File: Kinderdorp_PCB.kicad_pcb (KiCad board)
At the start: 2 copper layers, 99.1 x 99.1 mm, 44 parts, among them Q1 2N7002_C306856, U1 AMS1117-3.3_C347222, U2 ESP32-C3-WROOM-02-N4(4MB)

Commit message: routing
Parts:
- moved RXD 34.6 mm to (155.6, 123.1)
- moved GND 32.2 mm to (159.7, 123.1)
- moved TXD 30.5 mm to (151.5, 123.0)
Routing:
- net +5V: track 14.4 -> 325.1 mm, vias 0 -> 2
- net GPIO5: track 0.00 -> 100.7 mm, vias 0 -> 1
- net Net-(U2-IO2): track 0.00 -> 70.2 mm, vias 0 -> 1
- net Net-(LED4-DOUT): track 0.00 -> 47.4 mm
- net +3V3: track 83.4 -> 123.7 mm
- net Net-(LED2-DOUT): track 0.00 -> 38.5 mm
- net Net-(LED5-DOUT): track 0.00 -> 37.7 mm
- net Net-(LED7-DOUT): track 0.00 -> 35.6 mm
- net Net-(LED1-DOUT): track 0.00 -> 34.1 mm
- net Net-(LED6-DOUT): track 0.00 -> 32.3 mm
- net Net-(LED3-DOUT): track 0.00 -> 26.7 mm
- net Net-(U2-TXD): track 0.00 -> 18.4 mm
- net Net-(U2-RXD): track 0.00 -> 14.9 mm
- net BUZZ: track 13.9 -> 19.1 mm, vias 0 -> 2
- net Net-(D1-A): track 140.3 -> 138.3 mm

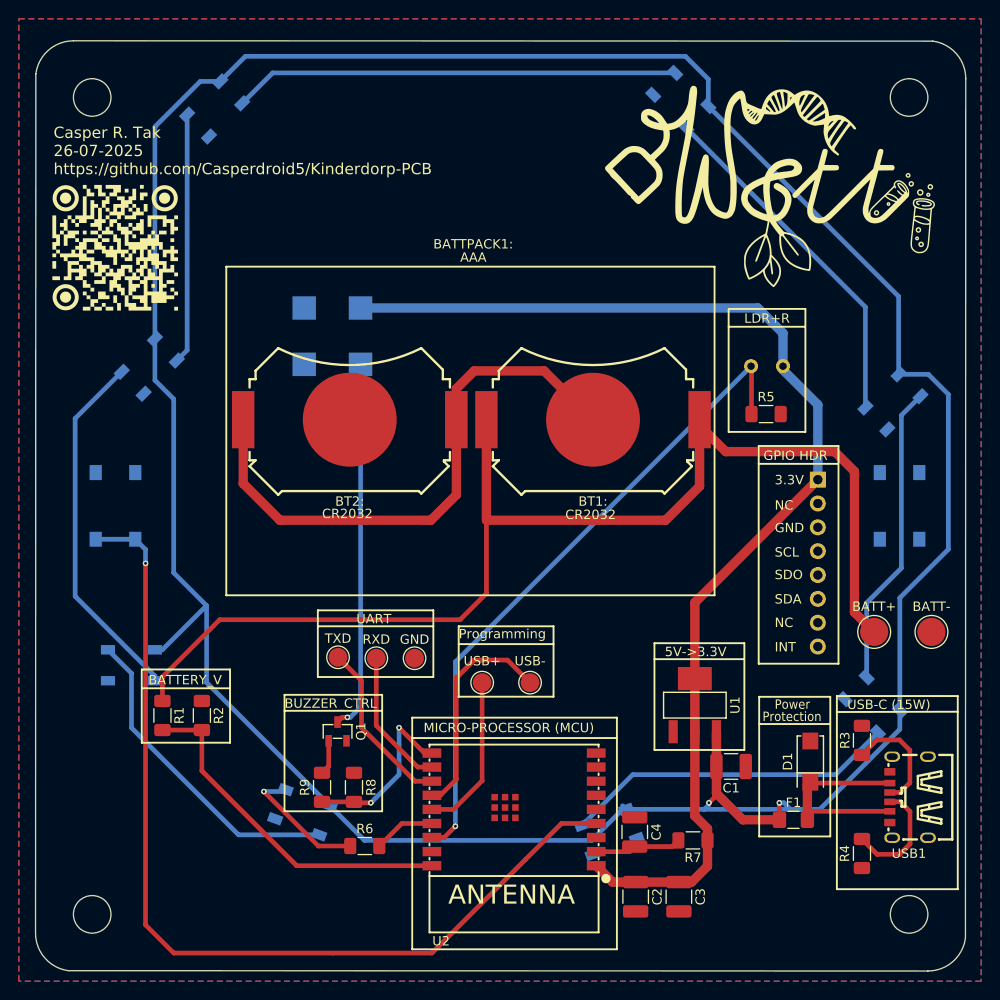
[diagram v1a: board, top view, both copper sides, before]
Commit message: added media files and finished routing
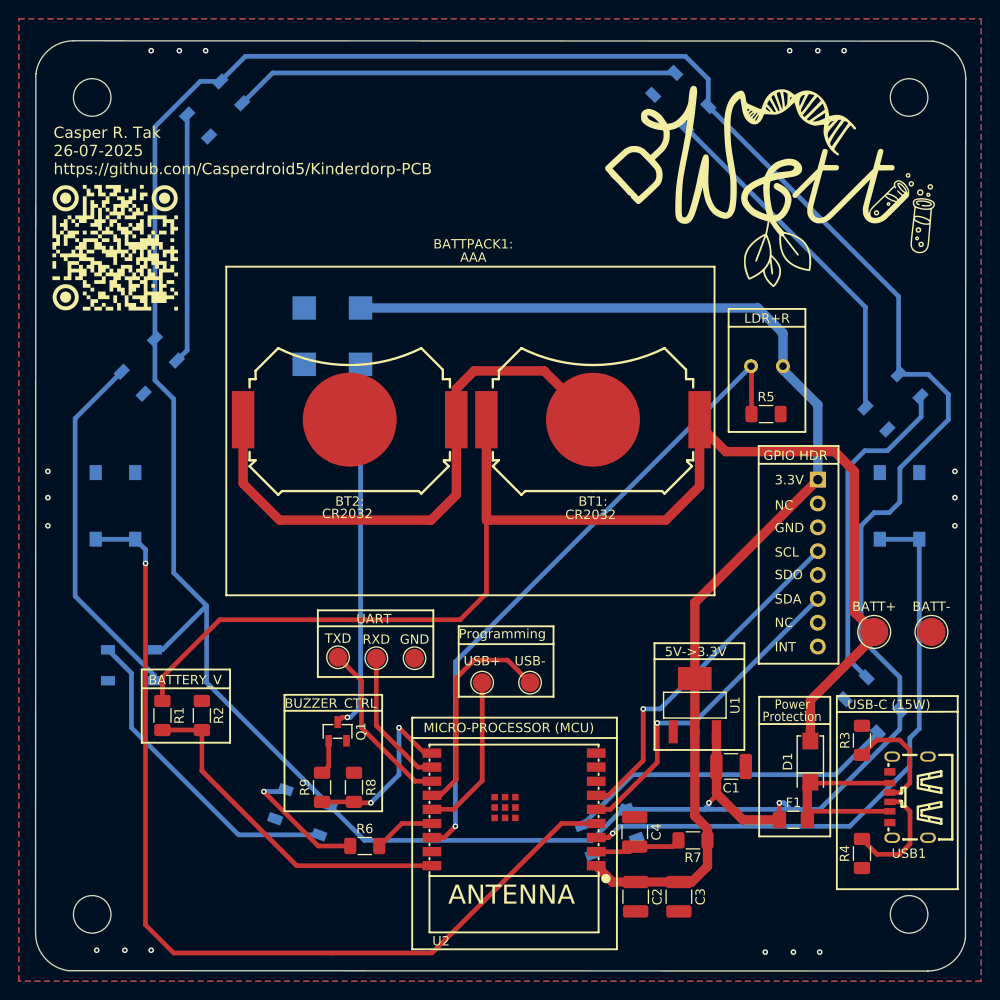
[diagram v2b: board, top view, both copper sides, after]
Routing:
- net GPIO4: track 0.00 -> 65.3 mm, vias 0 -> 1
- net GPIO7: track 0.00 -> 37.6 mm, vias 0 -> 1
- net GPIO6: track 0.00 -> 35.3 mm, vias 0 -> 1
- net Net-(D1-A): track 138.3 -> 152.8 mm
- net +5V: track 325.1 -> 329.5 mm
- net Net-(LED6-DOUT): track 32.3 -> 35.4 mm
- net GND: vias 0 -> 18

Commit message: Finalized design
- added esd protection
- minor silkscreen improvements
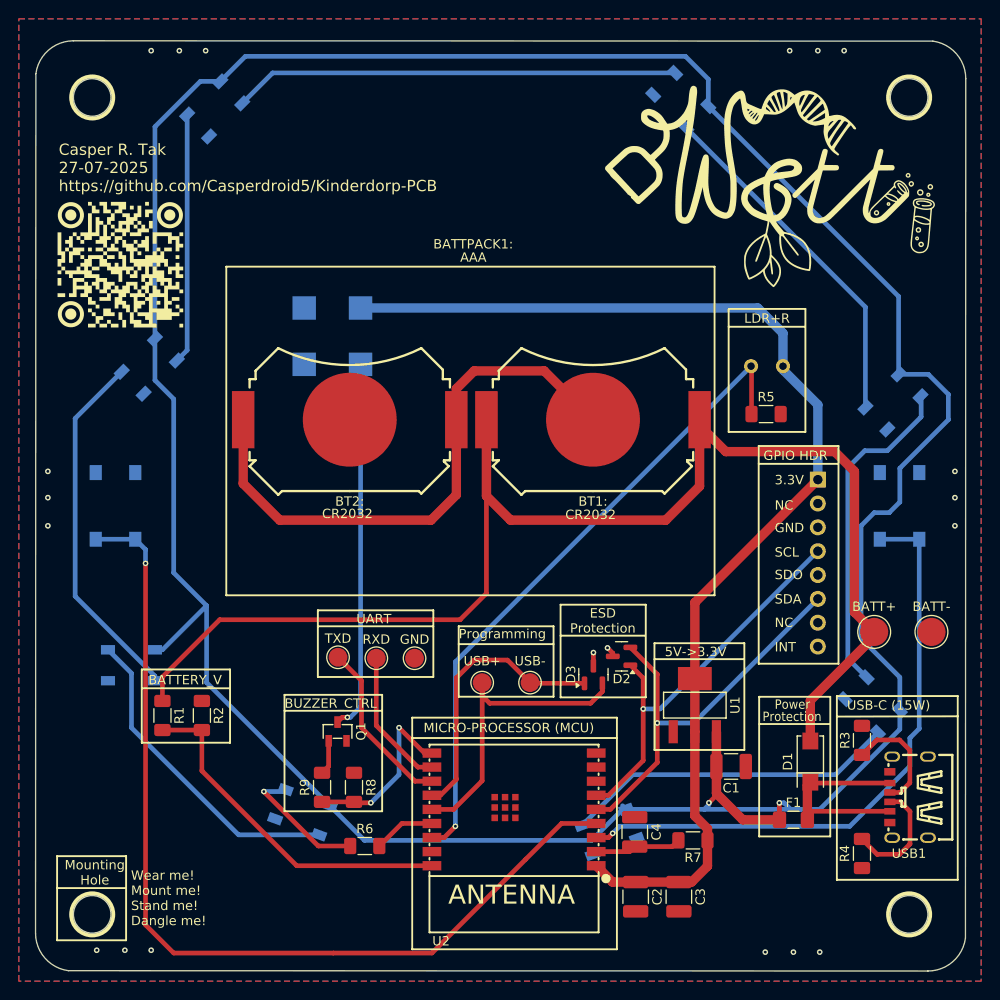
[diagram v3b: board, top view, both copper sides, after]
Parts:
- added D2: SM712_SOT23, Package_TO_SOT_SMD:SOT-23, F.Cu at (181.7, 122.9)
- added D3: SM712_SOT23, Package_TO_SOT_SMD:SOT-23, F.Cu at (178.7, 124.8)
- moved G*** 1.89 mm to (128.3, 81.2)
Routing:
- net D+_USB: track 17.1 -> 33.0 mm
- net GPIO6: track 35.3 -> 44.6 mm
- net D-_USB: track 23.7 -> 29.6 mm
- net GPIO7: track 37.6 -> 42.8 mm
- net GND: track 0.00 -> 2.53 mm, vias 18 -> 20
- net Net-(D1-A): track 152.8 -> 151.3 mm
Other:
- board text added: "Casper R. Tak 27-07-2025 https://github.com/Casperdroid5/Kinderdorp-PCB"
- board text added: "ESD Protection"
- board text added: "Mounting Hole"
- board text added: "Wear me! Mount me! Stand me! Dangle me!"
- board text removed: "Casper R. Tak 26-07-2025 https://github.com/Casperdroid5/Kinderdorp-PCB"

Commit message: minor changes to files and added production files
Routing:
- net GND: vias 20 -> 22
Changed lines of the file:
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@@
 	(paper "A4")
 	(title_block
-		(title "BirtydayCard")
-		(date "2025-05-12")
+		(title "Kinderdorp_PCB")
+		(date "2025-07-27")
 		(rev "V1")
 		(comment 1 "Casper R. Tak")
@@
 	)
 	(via
+		(at 187.3 137.27)
+		(size 0.6)
+		(drill 0.3)
+		(layers "F.Cu" "B.Cu")
+		(free yes)
+		(net 1)
+	)
+	(via
 		(at 180.2 122)
 		(size 0.6)
@@
 		(size 0.6)
 		(drill 0.3)
+		(layers "F.Cu" "B.Cu")
+		(free yes)
+		(net 1)
+	)
+	(via
+		(at 195.8 137.35)
+		(size 0.6)
+		(drill 0.3)

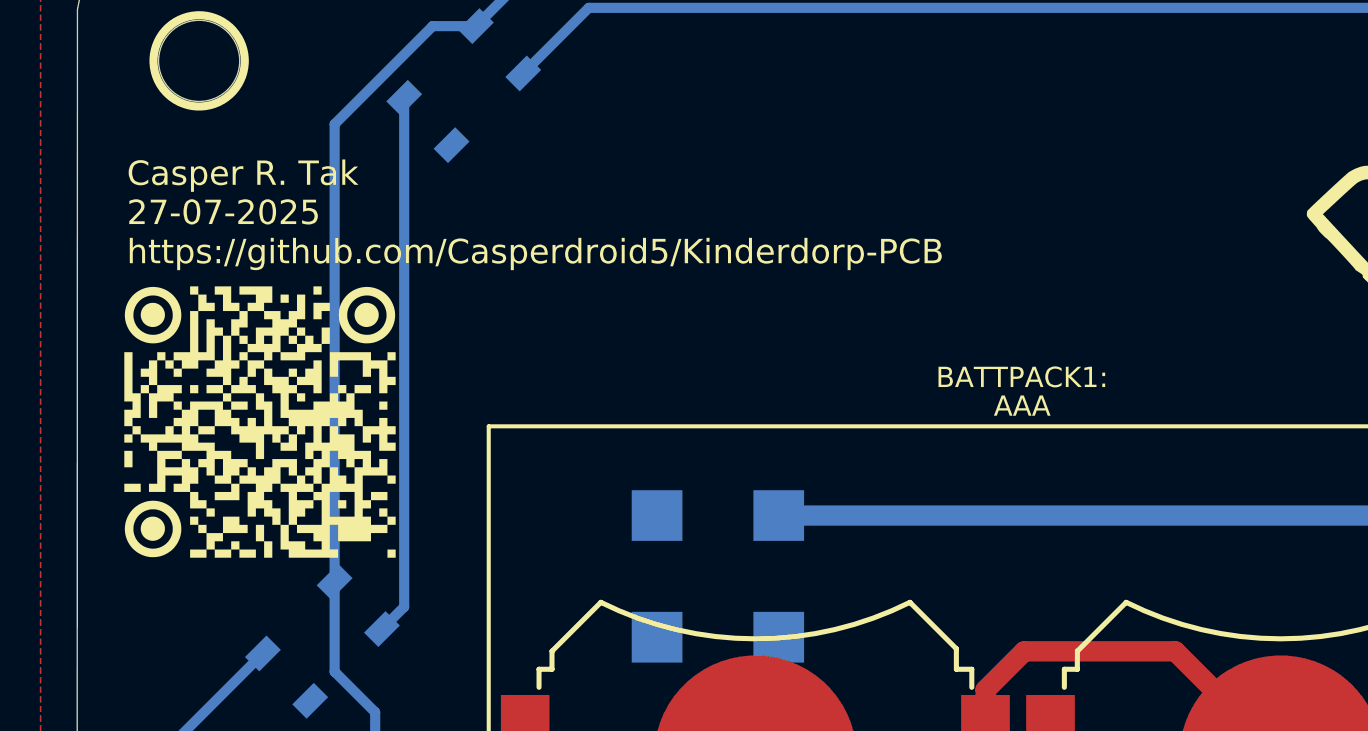
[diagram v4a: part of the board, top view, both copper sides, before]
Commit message: updated silkscreen
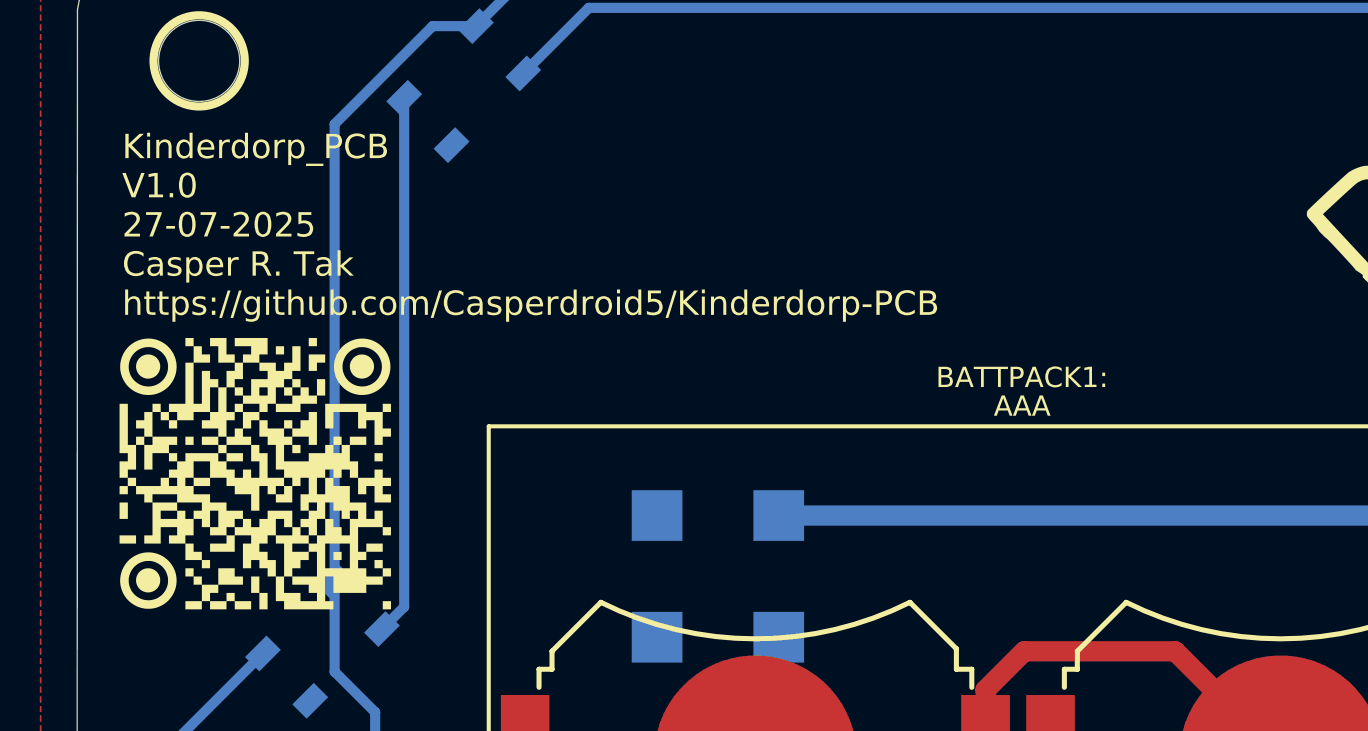
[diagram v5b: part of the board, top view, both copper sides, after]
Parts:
- moved G*** 2.56 mm to (128.1, 83.7)
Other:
- board text added: "Kinderdorp_PCB V1.0 27-07-2025 Casper R. Tak https://github.com/Casperdroid5/Kinderdorp-PCB"
- board text removed: "Casper R. Tak 27-07-2025 https://github.com/Casperdroid5/Kinderdorp-PCB"
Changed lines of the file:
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@@
 	(footprint "LOGO"
 		(layer "F.Cu")
-		(at 128.32 81.19)
+		(at 128.088279 83.735925)
 		(property "Reference" "G***"
 			(at 0 0 0)
@@
 		)
 	)
-	(gr_text "Casper R. Tak\n27-07-2025\nhttps://github.com/Casperdroid5/Kinderdorp-PCB"
-		(at 121.751721 73.504075 0)
+	(gr_text "Kinderdorp_PCB\nV1.0\n27-07-2025\nCasper R. Tak\nhttps://github.com/Casperdroid5/Kinderdorp-PCB"
+		(at 121.52 76.05 0)
 		(layer "F.SilkS")
 		(effects
